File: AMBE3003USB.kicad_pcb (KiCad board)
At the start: 2 copper layers, 64 x 64.3 mm, 96 parts, among them J1 McBSP, J2 ACONF, J3 CODEC, J4 USB_OTG, P1 CONN_02X16, U1 AMBE3003, U2 LD1117S33TR, U3 TPS3805, U4 FT232RL, U5 TPS78319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

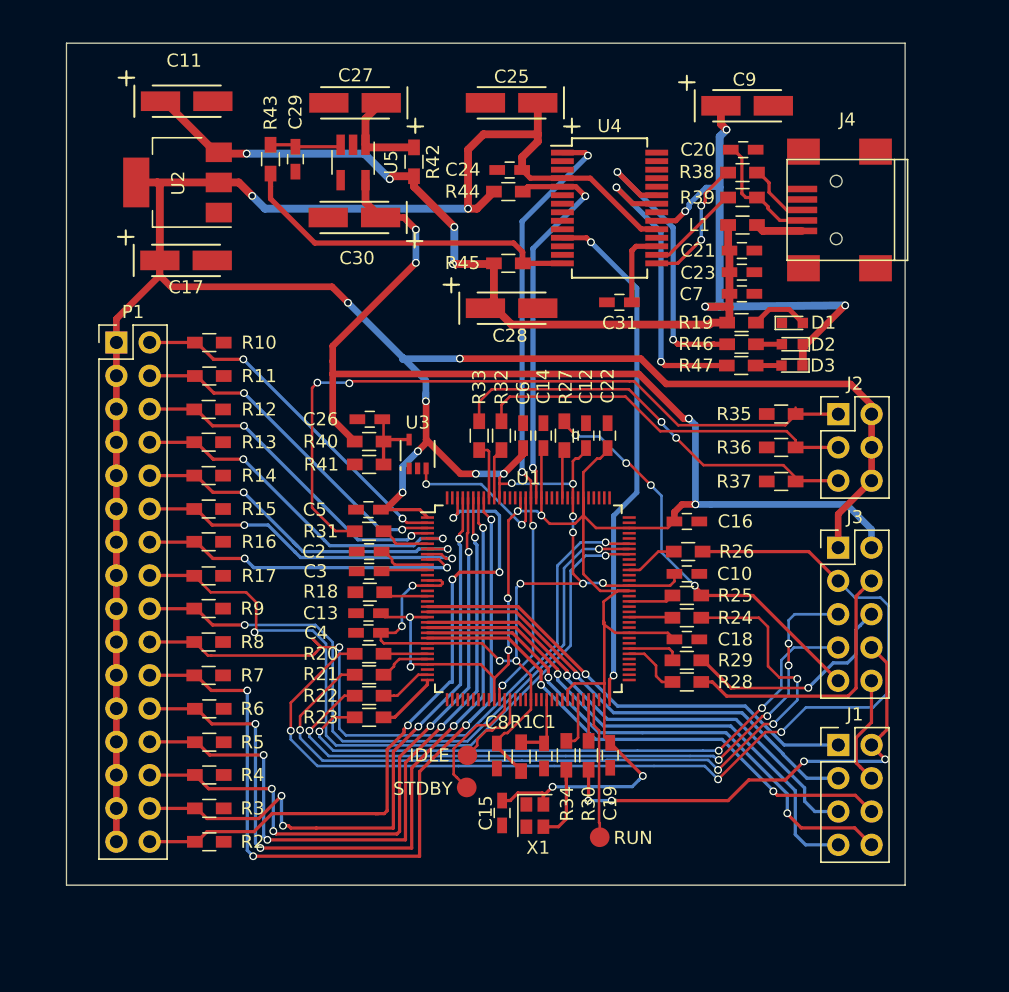
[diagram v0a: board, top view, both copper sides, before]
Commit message: Add GND zones
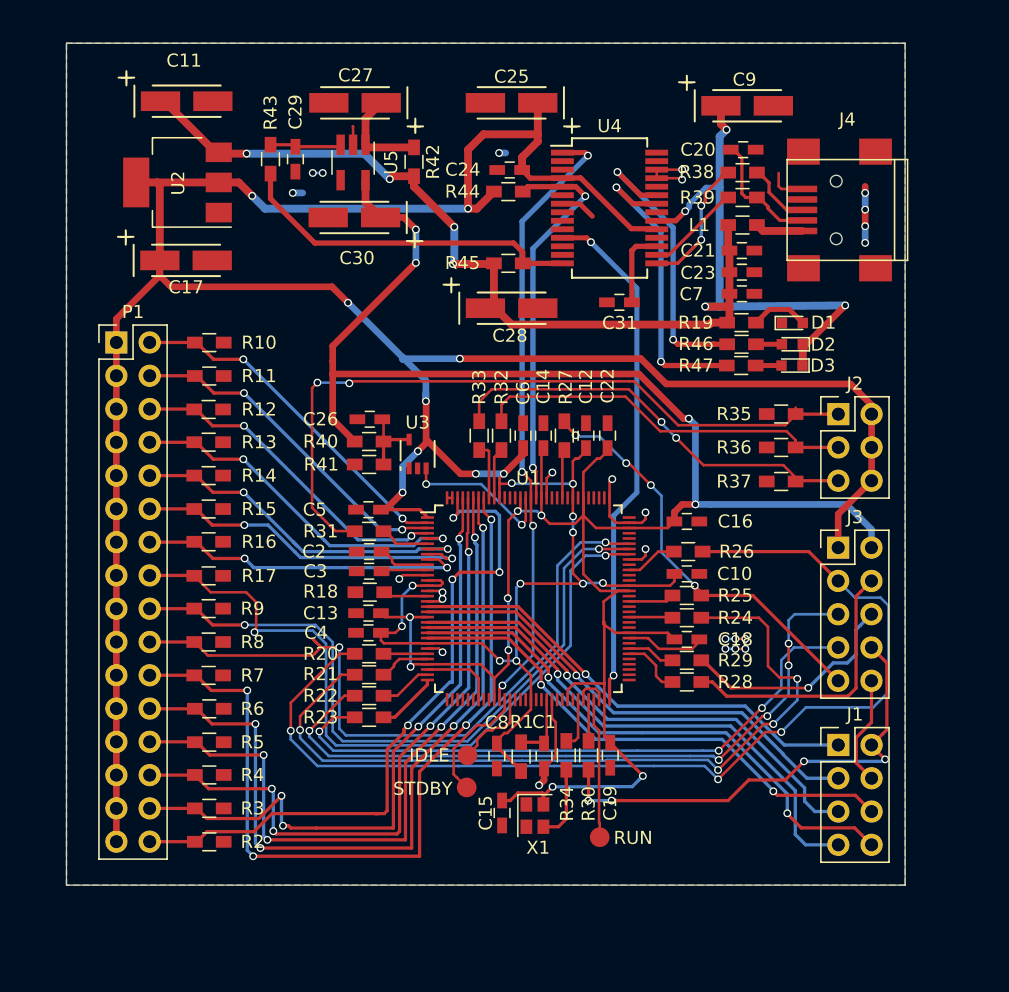
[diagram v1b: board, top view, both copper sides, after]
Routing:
- net GND: track 8.41 -> 59.0 mm, vias 0 -> 11
- net (no net): track 0.00 -> 10.2 mm, vias 0 -> 14
- added copper zone on B.Cu, net GND
- added copper zone on F.Cu, net GND

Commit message: Refactor all unconnected pins
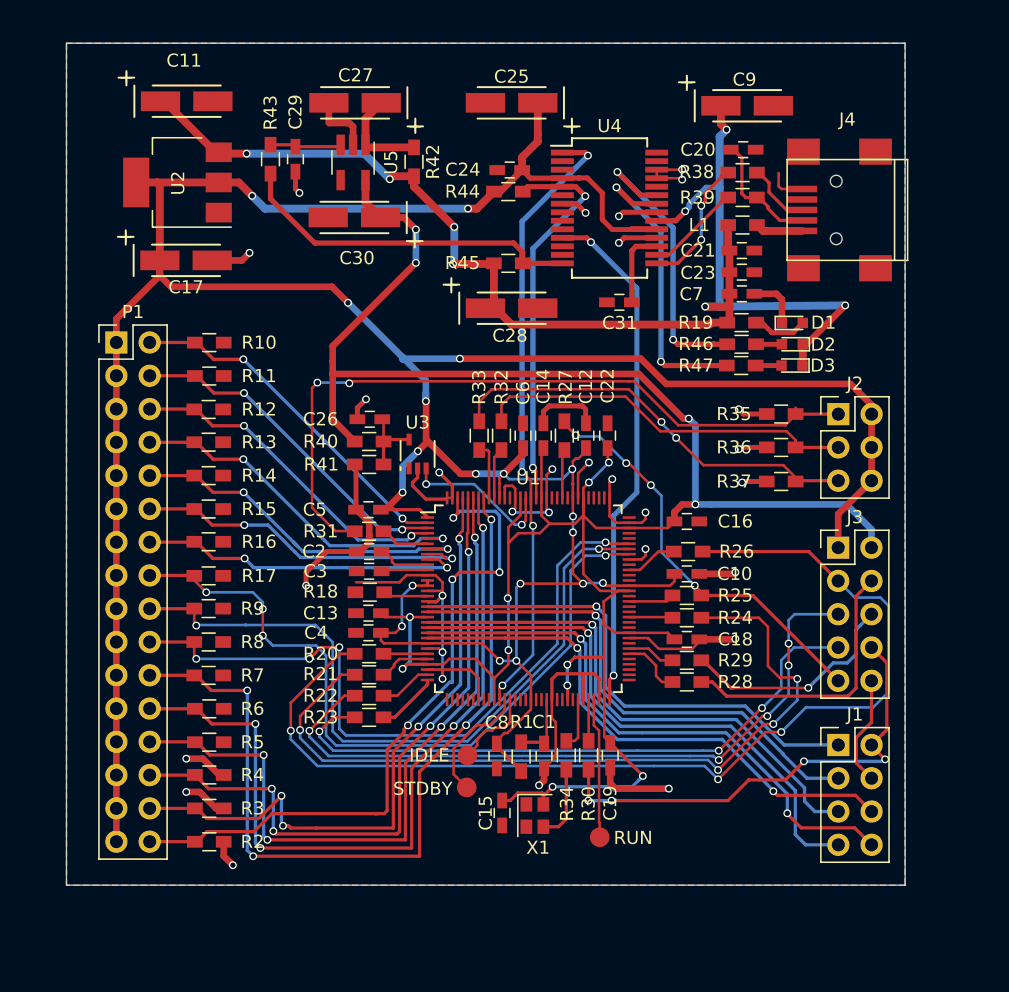
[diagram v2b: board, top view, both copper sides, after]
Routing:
- net GND: track 59.0 -> 162.4 mm, vias 11 -> 30
- net (no net): track 10.2 -> 0.00 mm, vias 14 -> 0
- net +3V3: track 277.4 -> 271.3 mm, vias 20 -> 19
- net +1V9: track 184.6 -> 190.3 mm, vias 12 -> 14
- net Net-(J1-Pad1): track 35.7 -> 39.1 mm
- net Net-(J1-Pad3): track 36.8 -> 39.9 mm
- net Net-(J1-Pad5): track 38.3 -> 41.0 mm
- net Net-(J1-Pad7): track 40.7 -> 43.1 mm
- net Net-(J1-Pad8): track 42.2 -> 44.2 mm
- net Net-(J1-Pad6): track 40.0 -> 42.0 mm
- net Net-(P1-Pad18): track 54.3 -> 55.2 mm
- net Net-(P1-Pad20): track 55.2 -> 54.3 mm, vias 2 -> 4
- net Net-(P1-Pad16): track 57.4 -> 57.0 mm, vias 2 -> 4

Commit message: Reorder some descriptors
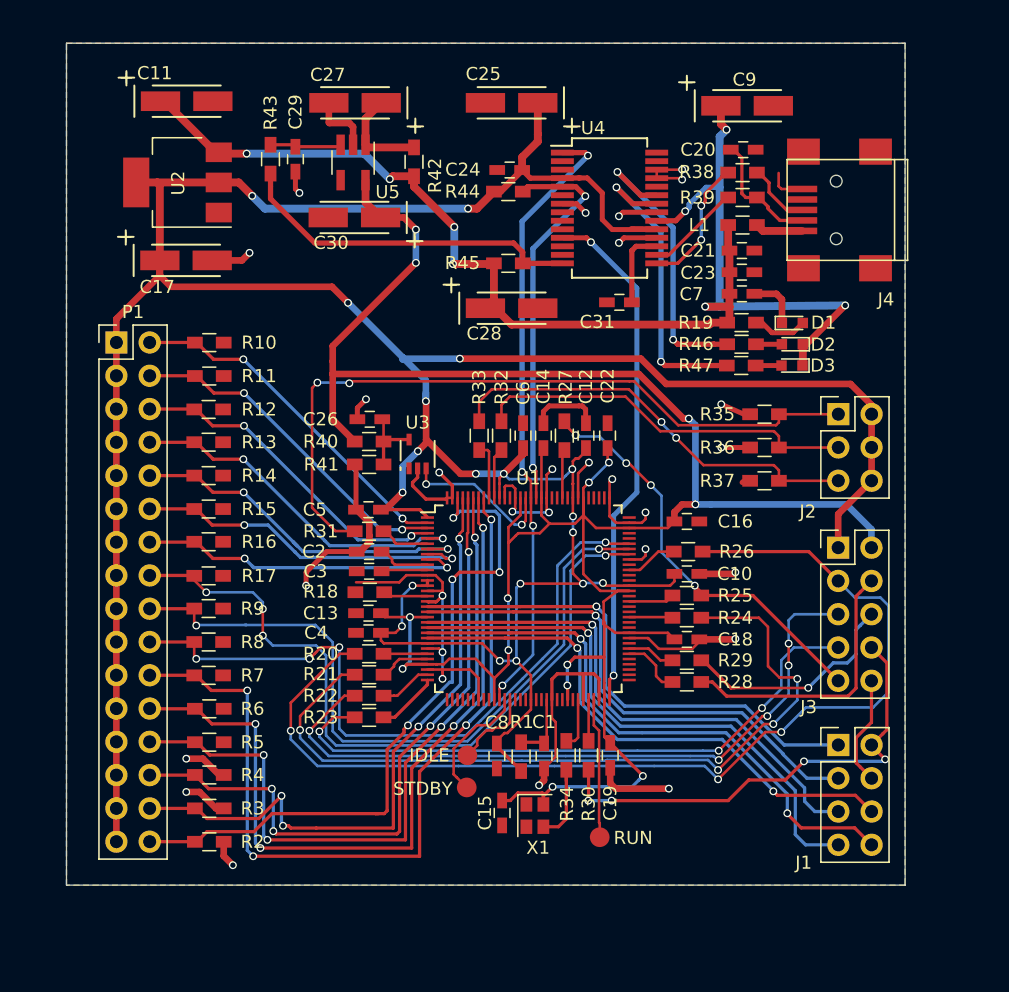
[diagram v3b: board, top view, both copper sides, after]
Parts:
- moved R37 1.27 mm to (104.1, 83.9)
- moved R35 1.27 mm to (104.1, 78.9)
- moved R36 1.27 mm to (104.1, 81.4)
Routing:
- net GND: track 162.4 -> 160.1 mm, vias 30 -> 29

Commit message: Rounded corners, added descriptors
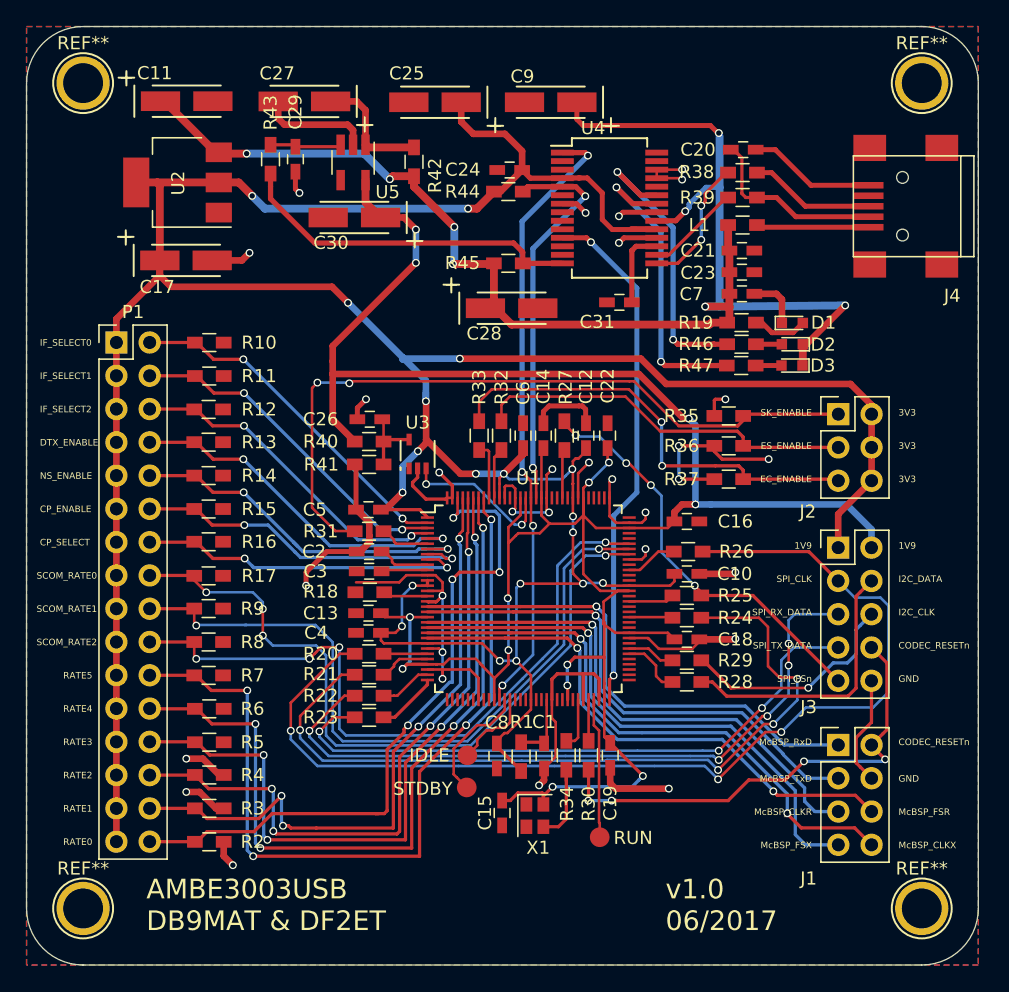
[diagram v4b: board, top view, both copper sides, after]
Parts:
- added REF**: 1pin, Connect:1pin, F.Cu at (52.1, 116.6)
- added REF**: 1pin, Connect:1pin, F.Cu at (52.1, 53.6)
- added REF**: 1pin, Connect:1pin, F.Cu at (116.1, 53.6)
- added REF**: 1pin, Connect:1pin, F.Cu at (116.1, 116.6)
- P1: value CONN_02X16 -> CONFIG
- X1: value SG-210STF -> 29.4912
- moved C9 15.0 mm to (87.8, 55.1), turned to 180 degrees
- moved C25 5.84 mm to (78.9, 55.1)
- moved J4 5.07 mm to (114.8, 63.0)
- moved C27 3.87 mm to (69.0, 55.0)
- moved R37 2.73 mm to (101.3, 83.8)
- moved R35 2.73 mm to (101.3, 79.0)
- moved R36 2.73 mm to (101.3, 81.3)
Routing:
- net GND: track 160.1 -> 181.3 mm, vias 29 -> 31
- net +5V: track 104.8 -> 114.9 mm
- net Net-(C20-Pad1): track 9.37 -> 14.4 mm
- net Net-(J4-Pad1): track 3.64 -> 8.58 mm
- net Net-(J4-Pad3): track 5.06 -> 9.72 mm
- net +3V3: track 271.3 -> 274.2 mm
- net Net-(J2-Pad5): track 32.7 -> 34.7 mm
- net Net-(C27-Pad1): track 7.48 -> 9.36 mm
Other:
- board size 64 x 64.3 mm -> 72.6 x 71.6 mm
- board text added: "1V9"
- board text added: "3V3"
- board text added: "AMBE3003USB DB9MAT & DF2ET"
- board text added: "CODEC_RESETn"
- board text added: "CP_ENABLE"
- board text added: "CP_SELECT"
- board text added: "DTX_ENABLE"
- board text added: "EC_ENABLE"
- board text added: "ES_ENABLE"
- board text added: "GND"
- board text added: "I2C_CLK"
- board text added: "I2C_DATA"
- board text added: "IF_SELECT0"
- board text added: "IF_SELECT1"
- board text added: "IF_SELECT2"
- board text added: "McBSP_CLKR"
- board text added: "McBSP_CLKX"
- board text added: "McBSP_FSR"
- board text added: "McBSP_FSX"
- board text added: "McBSP_RxD"
- board text added: "McBSP_TxD"
- board text added: "NS_ENABLE"
- board text added: "RATE0"
- board text added: "RATE1"
- board text added: "RATE2"
- board text added: "RATE3"
- board text added: "RATE4"
- board text added: "RATE5"
- board text added: "SCOM_RATE0"
- board text added: "SCOM_RATE1"
- board text added: "SCOM_RATE2"
- board text added: "SK_ENABLE"
- board text added: "SPI_CLK"
- board text added: "SPI_FSn"
- board text added: "SPI_RX_DATA"
- board text added: "SPI_TX_DATA"
- board text added: "v1.0 06/2017"

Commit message: Add OSHW logo and realign jumpers
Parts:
- added G***: LOGO, OPENHARDWARE:OSHWLOGO0.3IN, F.Cu at (97.0, 111.5)
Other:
- board text removed: "3V3"

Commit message: Added nice net names / labels
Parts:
- removed STDBY: TEST, Measurement_Points:Measurement_Point_Round-SMD-Pad_Small
- added STANDBY: TP1, Measurement_Points:Measurement_Point_Round-SMD-Pad_Small, F.Cu at (81.3, 107.3)
- IDLE: value TEST -> TP2
- RUN: value TEST -> TP3
- moved RUN 0.19 mm to (91.3, 111.1)
- moved IDLE 0.13 mm to (81.4, 105.0)
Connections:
- net Net-(C1-Pad1) renamed /_3V3FL
- net Net-(C2-Pad1) renamed /_VREF_1V
- net Net-(C3-Pad1) renamed /_VREF_2V
- net Net-(J1-Pad1) renamed /_McBSP_RxD
- net Net-(J1-Pad3) renamed /_McBSP_TxD
- net Net-(J1-Pad5) renamed /_McBSP_CLKR
- net Net-(J1-Pad6) renamed /_McBSP_FSR
- net Net-(J1-Pad7) renamed /_McBSP_FSX
- net Net-(J1-Pad8) renamed /_McBSP_CLKX
- net Net-(P1-Pad10) renamed /_NS_ENABLE
- net Net-(P1-Pad12) renamed /_CP_ENABLE
- net Net-(P1-Pad14) renamed /_CP_SELECT
- net Net-(P1-Pad16) renamed /_S_COM_RATE0
- net Net-(P1-Pad18) renamed /_S_COM_RATE1
- net Net-(P1-Pad2) renamed /_IF_SELECT0
- net Net-(P1-Pad20) renamed /_S_COM_RATE2
- net Net-(P1-Pad22) renamed /_RATE5
- net Net-(P1-Pad24) renamed /_RATE4
- net Net-(P1-Pad26) renamed /_RATE3
- net Net-(P1-Pad28) renamed /_RATE2
- net Net-(P1-Pad30) renamed /_RATE1
- net Net-(P1-Pad32) renamed /_RATE0
- net Net-(P1-Pad4) renamed /_IF_SELECT1
- net Net-(P1-Pad6) renamed /_IF_SELECT2
- net Net-(P1-Pad8) renamed /_DTX_ENABLE
- net Net-(R18-Pad2) renamed /ADCRESEXT
- net Net-(R20-Pad2) renamed /_SPI_CLK
- net Net-(R21-Pad2) renamed /_SPI_STE
- net Net-(R22-Pad2) renamed /_SPI_RX_DATA
- net Net-(R23-Pad2) renamed /_SPI_TX_DATA
- net Net-(R24-Pad2) renamed /_SPI_GENSTE
- net Net-(R25-Pad2) renamed /_SPI_FSn
- net Net-(R26-Pad2) renamed /_SPI_CLK_IN
- net Net-(R27-Pad2) renamed /_SPI_WAKE
- net Net-(R28-Pad2) renamed /_I2C_DATA
- net Net-(R29-Pad2) renamed /_I2C_CLK
- net Net-(R30-Pad2) renamed /_CODEC_RESETn
- net Net-(R31-Pad2) renamed /_SK_ENABLE
- net Net-(R32-Pad2) renamed /_ES_ENABLE
- net Net-(R33-Pad2) renamed /_EC_ENABLE
- net Net-(TP2-Pad1) renamed /_IDLE
- net Net-(TP3-Pad1) renamed /_RUN
- U1 pad 44: Net-(TP1-Pad1) -> /_STANDBY
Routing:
- net Net-(TP1-Pad1): track 9.29 -> 0.00 mm
- net /_STANDBY: track 0.00 -> 9.29 mm

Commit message: Add some more labels
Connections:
- net Net-(C20-Pad1) renamed /D-
- net Net-(J2-Pad1) renamed /SK_ENABLE
- net Net-(J2-Pad3) renamed /ES_ENABLE
- net Net-(J2-Pad5) renamed /EC_ENABLE
- net Net-(J4-Pad1) renamed /VBUS
- net Net-(J4-Pad3) renamed /D+
- net Net-(R34-Pad2) renamed /_X1/CLKIN

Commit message: Refactor schematic (moved C24)
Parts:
- L1: value L_Small -> 100MHz
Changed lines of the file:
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@@
       (effects (font (size 1 1) (thickness 0.15)))
     )
-    (fp_text value L_Small (at -4.8515 -0.091 180) (layer F.Fab)
+    (fp_text value 100MHz (at -4.8515 -0.091 180) (layer F.Fab)
       (effects (font (size 1 1) (thickness 0.15)))
     )
